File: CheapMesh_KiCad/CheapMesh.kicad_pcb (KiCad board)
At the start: 2 copper layers, 34.8 x 67.3 mm, 25 parts, among them J1 Conn_01x02_Pin, J2 Conn_01x09_Pin, J3 USB_A, J4 USB_C, J5 Conn_Coaxial, Q1 UMH3N, U1 L78L33, U2 HT-CT62, U3 AP2112K-3.3

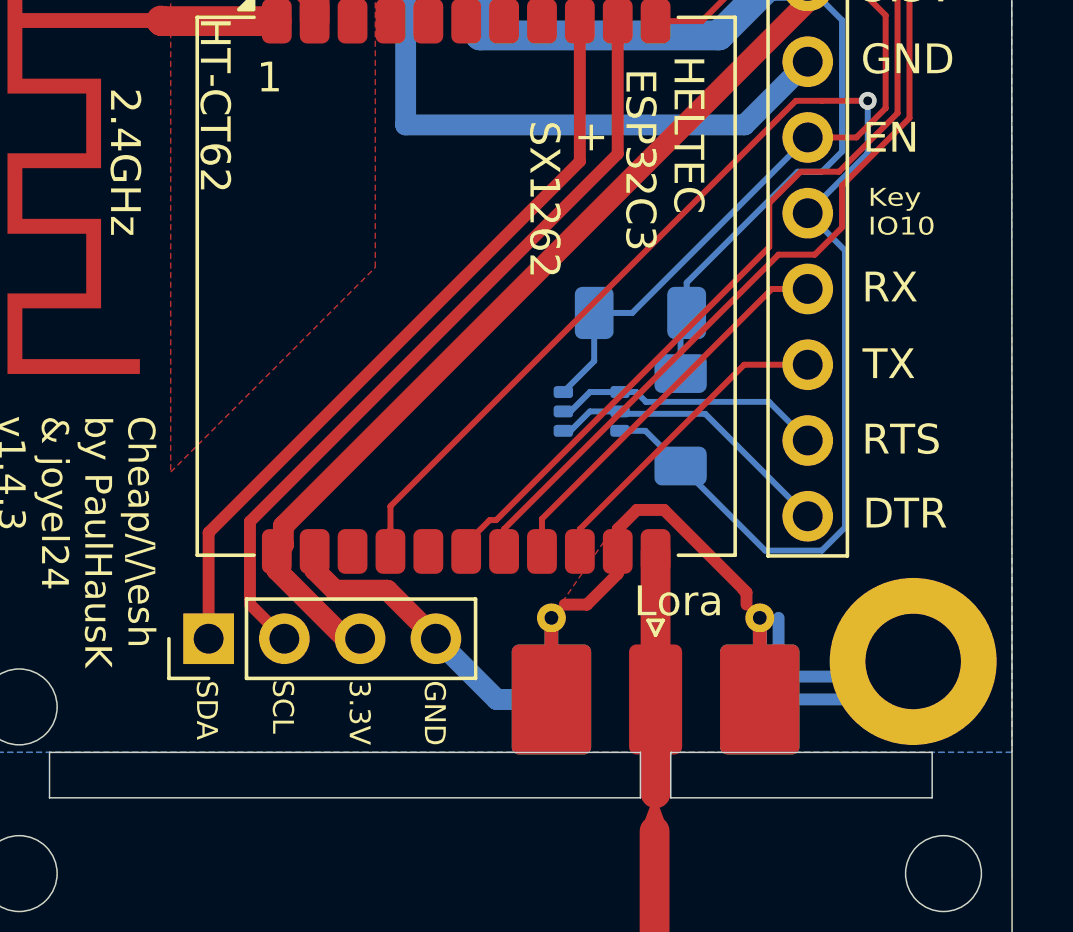
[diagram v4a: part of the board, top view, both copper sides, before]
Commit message: GPIO num visible on PC
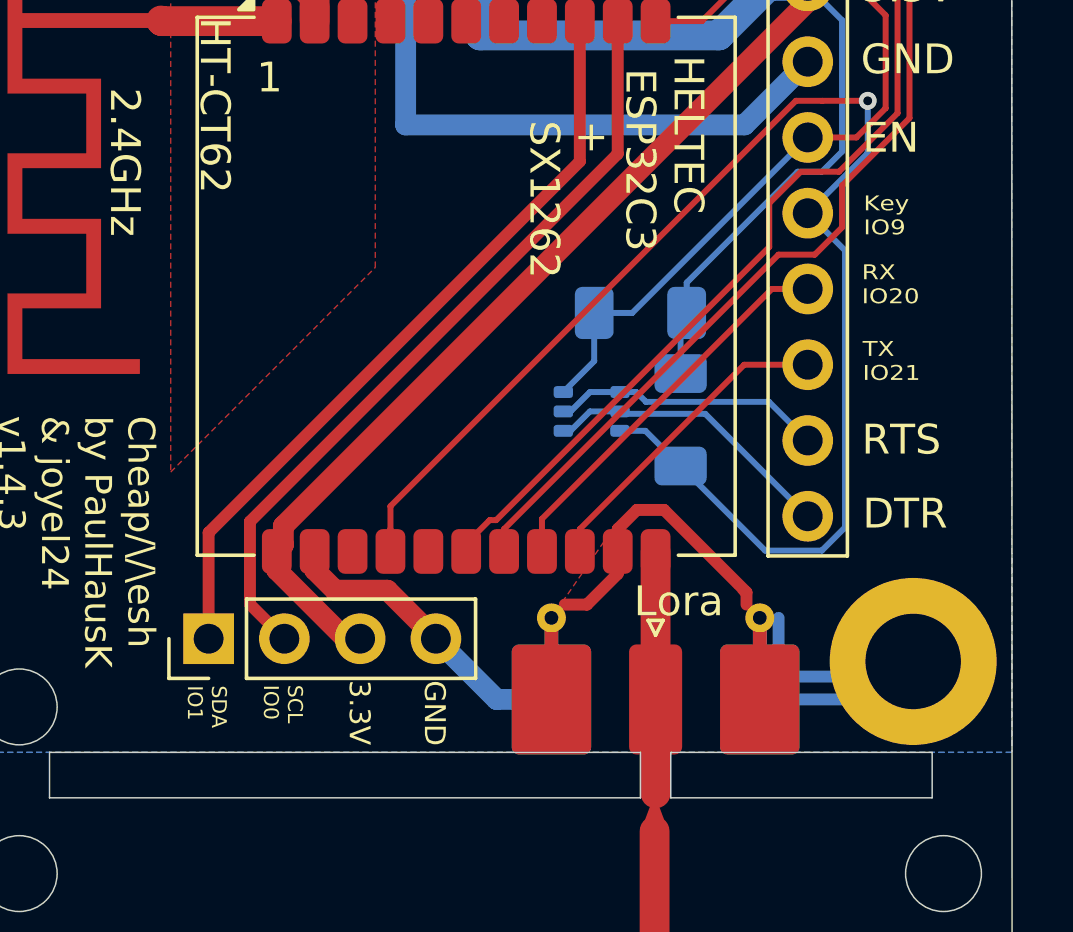
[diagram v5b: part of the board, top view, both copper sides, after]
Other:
- board text added: "Key IO9"
- board text added: "RX IO20"
- board text added: "SCL IO0"
- board text added: "SDA IO1"
- board text added: "TX IO21"
- board text removed: "Key IO10"
- board text removed: "RX"
- board text removed: "SCL"
- board text removed: "SDA"
- board text removed: "TX"
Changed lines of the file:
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@@
 		)
 	)
-	(gr_text "TX"
+	(gr_text "TX\nIO21"
 		(at 62.82 148.61 0)
 		(layer "F.SilkS")
 		(effects
 			(font
-				(size 1 1)
+				(size 0.5 0.6)
 				(thickness 0.1)
 			)
@@
 		)
 	)
-	(gr_text "SCL"
-		(at 42.97 158.6 270)
+	(gr_text "SCL\nIO0"
+		(at 42.69 158.77 270)
 		(layer "F.SilkS")
 		(effects
 			(font
-				(size 0.7 0.7)
+				(size 0.5 0.5)
 				(thickness 0.07)
 			)
@@
 		)
 	)
-	(gr_text "SDA"
-		(at 40.42 158.62 270)
+	(gr_text "SDA\nIO1\n"
+		(at 40.14 158.79 270)
 		(layer "F.SilkS")
 		(effects
 			(font
-				(size 0.7 0.7)
+				(size 0.5 0.5)
 				(thickness 0.07)
 			)
@@
 		)
 	)
-	(gr_text "Key\nIO10"
-		(at 63 143.75 0)
+	(gr_text "Key\nIO9"
+		(at 62.85 143.73 0)
 		(layer "F.SilkS")
 		(effects
 			(font
-				(size 0.6 0.7)
+				(size 0.5 0.6)
 				(thickness 0.1)
 			)
@@
 		)
 	)
-	(gr_text "RX"
+	(gr_text "RX\nIO20"
 		(at 62.79 146.04 0)
 		(layer "F.SilkS")
 		(effects
 			(font
-				(size 1 1)
+				(size 0.5 0.6)
 				(thickness 0.1)
 			)

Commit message: update version
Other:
- board text added: "Cheap/\/\esh by PaulHausK & joyel24 v1.4.4"
- board text removed: "Cheap/\/\esh by PaulHausK & joyel24 v1.4.3"
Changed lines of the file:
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@@
 		)
 	)
-	(gr_text "Cheap/\\/\\esh\nby PaulHausK\n& joyel24\nv1.4.3\n"
+	(gr_text "Cheap/\\/\\esh\nby PaulHausK\n& joyel24\nv1.4.4\n"
 		(at 33.75 149.75 270)
 		(layer "F.SilkS")
